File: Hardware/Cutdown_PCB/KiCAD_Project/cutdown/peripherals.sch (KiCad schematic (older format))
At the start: 14 parts, among them Q1 MMBT3904, U2 BMP388, U3 ublox_SAM-M8Q

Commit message: Cutdown PCB Rev 1.0 Complete.
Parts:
- R13: Populated 0 -> 1
- R9: value 10k -> NP
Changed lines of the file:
@@
 AR Path="/5DE92E14/5DE9BB83" Ref="R9"  Part="1"
 F 0 "R9" V 2725 2350 50  0000 L CNN
-F 1 "10k" V 2825 2325 50  0000 L CNN
+F 1 "NP" V 2825 2350 50  0000 L CNN
 F 2 "Resistors_SMD:R_0603_HandSoldering" V 2755 2400 50  0001 C CNN
 F 3 "~" H 2825 2400 50  0001 C CNN
@@
 F 3 "~" H 4725 2250 50  0001 C CNN
 F 4 "1-0000010" H 4725 2250 50  0001 C CNN "Internal Part Number"
-F 5 "0" H 4725 2250 50  0001 C CNN "Populated"
+F 5 "1" H 4725 2250 50  0001 C CNN "Populated"
 	1    4725 2250
 	1    0    0    -1

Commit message: Fix GPS connection to particle.
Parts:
- R10, R11, R12, R13, R9: footprint Resistors_SMD:R_0603_HandSoldering -> Resistor_SMD:R_0603_1608Metric_Pad1.05x0.95mm_HandSolder
- U3: symbol cutdown-rescue:ublox_SAM-M8Q-RF_GPS -> lib_sch:ublox_SAM-M8Q
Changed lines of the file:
@@
 EESchema Schematic File Version 4
-LIBS:cutdown-cache
 EELAYER 30 0
 EELAYER END
@@
 Sheet 2 2
 Title "Cutdown Module - NSSL EFM"
-Date "2019-12-03"
-Rev "1.0"
+Date "2020-03-30"
+Rev "2.0"
 Comp "Leeman Geophysical LLC"
 Comment1 "(479) 373-3736"
@@
 F 0 "R9" V 2725 2350 50  0000 L CNN
 F 1 "NP" V 2825 2350 50  0000 L CNN
-F 2 "Resistors_SMD:R_0603_HandSoldering" V 2755 2400 50  0001 C CNN
+F 2 "Resistor_SMD:R_0603_1608Metric_Pad1.05x0.95mm_HandSolder" V 2755 2400 50  0001 C CNN
 F 3 "~" H 2825 2400 50  0001 C CNN
 F 4 "1-0000010" H 2825 2400 50  0001 C CNN "Internal Part Number"
@@
 F 0 "R10" V 2725 2750 50  0000 L CNN
 F 1 "10k" V 2825 2725 50  0000 L CNN
-F 2 "Resistors_SMD:R_0603_HandSoldering" V 2755 2800 50  0001 C CNN
+F 2 "Resistor_SMD:R_0603_1608Metric_Pad1.05x0.95mm_HandSolder" V 2755 2800 50  0001 C CNN
 F 3 "~" H 2825 2800 50  0001 C CNN
 F 4 "1-0000010" H 2825 2800 50  0001 C CNN "Internal Part Number"
@@
 GPS_TX
 $Comp
-L cutdown-rescue:ublox_SAM-M8Q-RF_GPS U3
+L lib_sch:ublox_SAM-M8Q U3
 U 1 1 5DE9BBA4
 P 7200 2425
@@
 F 0 "R12" V 5700 4550 50  0000 L CNN
 F 1 "1k" V 5775 4550 50  0000 L CNN
-F 2 "Resistors_SMD:R_0603_HandSoldering" V 5705 4600 50  0001 C CNN
+F 2 "Resistor_SMD:R_0603_1608Metric_Pad1.05x0.95mm_HandSolder" V 5705 4600 50  0001 C CNN
 F 3 "~" H 5775 4600 50  0001 C CNN
 F 4 "1-0000013" H 5775 4600 50  0001 C CNN "Internal Part Number"
@@
 F 0 "R11" V 5250 5000 50  0000 L CNN
 F 1 "1k" V 5325 5000 50  0000 L CNN
-F 2 "Resistors_SMD:R_0603_HandSoldering" V 5255 5050 50  0001 C CNN
+F 2 "Resistor_SMD:R_0603_1608Metric_Pad1.05x0.95mm_HandSolder" V 5255 5050 50  0001 C CNN
 F 3 "~" H 5325 5050 50  0001 C CNN
 F 4 "1-0000013" H 5325 5050 50  0001 C CNN "Internal Part Number"
@@
 F 0 "R13" V 4625 2200 50  0000 L CNN
 F 1 "10k" V 4725 2175 50  0000 L CNN
-F 2 "Resistors_SMD:R_0603_HandSoldering" V 4655 2250 50  0001 C CNN
+F 2 "Resistor_SMD:R_0603_1608Metric_Pad1.05x0.95mm_HandSolder" V 4655 2250 50  0001 C CNN
 F 3 "~" H 4725 2250 50  0001 C CNN
 F 4 "1-0000010" H 4725 2250 50  0001 C CNN "Internal Part Number"

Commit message: Rework cutdown schematic for version 2
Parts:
- removed BT1: CR1220, lib_fp:S8411-45R, symbol Device:Battery_Cell
- removed BZ1: Buzzer, lib_fp:PS1240P02BT, symbol Device:Buzzer
- removed C3, C4: 0.1u, Capacitors_SMD:C_0603_HandSoldering, symbol Device:C
- removed Q1: MMBT3904, TO_SOT_Packages_SMD:SOT-23, symbol Transistor_BJT:MMBT3904
- removed R11, R12: 1k, Resistor_SMD:R_0603_1608Metric_Pad1.05x0.95mm_HandSolder, symbol Device:R
- removed U3: ublox_SAM-M8Q, lib_fp:SAM-M8Q, symbol lib_sch:ublox_SAM-M8Q
- added BT? (x2): CR123, symbol Device:Battery_Cell
- added J?: Hot Wire, symbol Connector_Generic:Conn_01x02
- added Q?: FQP30N06L, Package_DirectFET:DirectFET_ST, symbol lib_sch:FQP30N06L
- added R?: 1-0000006, resistors_0603:1-0000006, symbol resistors_0603:1-0000006
- added R?: 1-0000010, resistors_0603:1-0000010, symbol resistors_0603:1-0000010
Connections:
- net labels added: Cutdown_Command
- net labels removed: +BATT, GPS_PPS, GPS_RX, GPS_TX, PIEZO_ELEMENT
- wire segments 30 -> 22
- no-connect marks 5 -> 0
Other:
- note added: "Required mating block\n1-0000784"

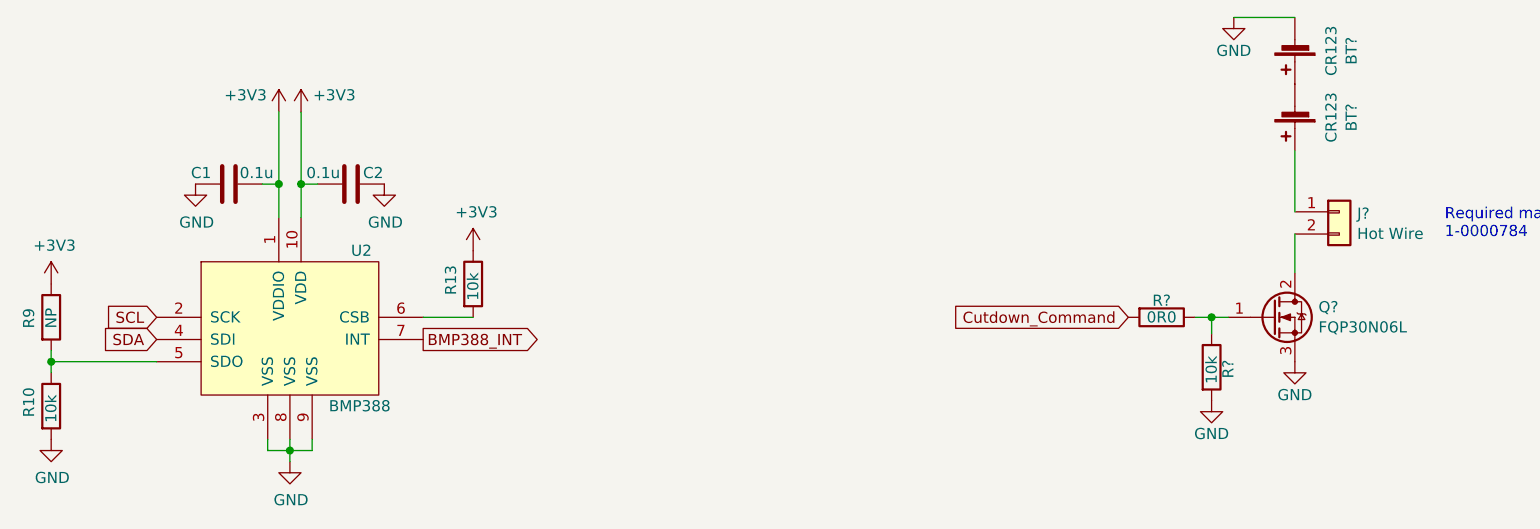
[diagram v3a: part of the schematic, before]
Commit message: Remove cutdown power pcb and update cutdown design
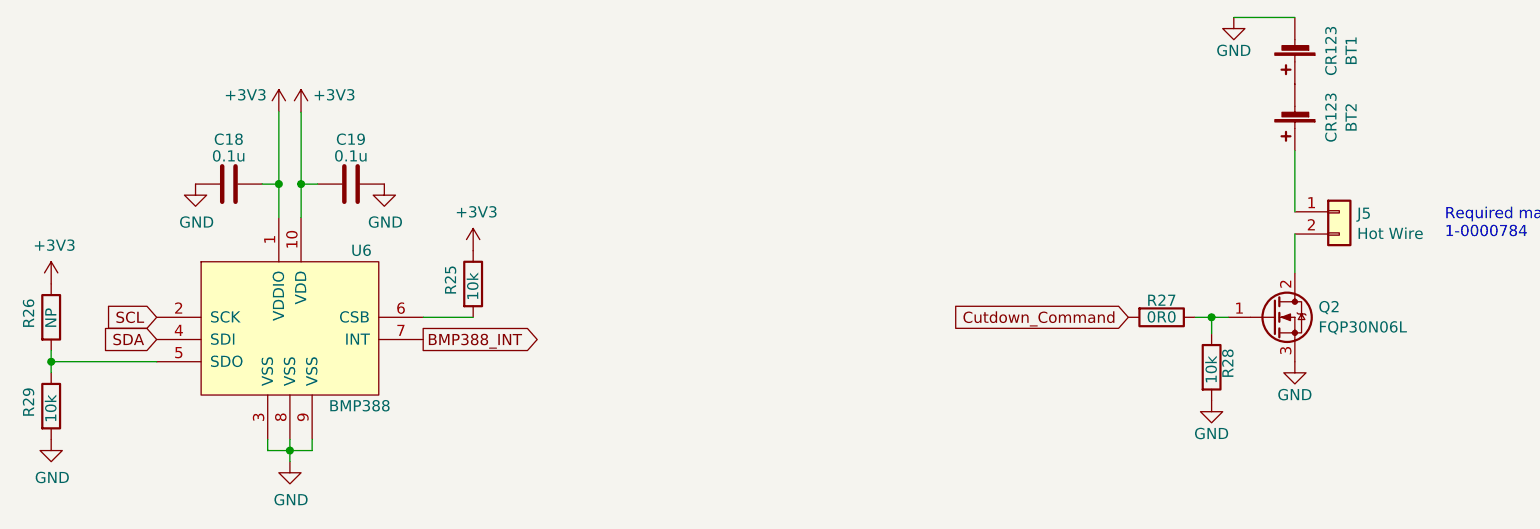
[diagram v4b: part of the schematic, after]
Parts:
- BT1, BT2: renamed from BT?; footprint (none) -> lib_fp:1-0000782
- C18: renamed from C1; footprint Capacitors_SMD:C_0603_HandSoldering -> Capacitor_SMD:C_0603_1608Metric
- C19: renamed from C2; footprint Capacitors_SMD:C_0603_HandSoldering -> Capacitor_SMD:C_0603_1608Metric
- J5: renamed from J?; footprint (none) -> lib_fp:1-0000783
- Q2: renamed from Q?; footprint Package_DirectFET:DirectFET_ST -> Package_TO_SOT_THT:TO-220-3_Horizontal_TabDown; Internal Part Number (none) -> 1-0000449; Populated (none) -> 1
- R25: renamed from R13; footprint Resistor_SMD:R_0603_1608Metric_Pad1.05x0.95mm_HandSolder -> Resistor_SMD:R_0603_1608Metric
- R26: renamed from R9; footprint Resistor_SMD:R_0603_1608Metric_Pad1.05x0.95mm_HandSolder -> Resistor_SMD:R_0603_1608Metric
- R29: renamed from R10; footprint Resistor_SMD:R_0603_1608Metric_Pad1.05x0.95mm_HandSolder -> Resistor_SMD:R_0603_1608Metric
- gave numbers to parts that had none: 2
- renumbered U2 to U6
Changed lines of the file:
@@
 Sheet 2 2
 Title "Cutdown Module - NSSL EFM"
-Date "2020-03-30"
-Rev "2.0"
+Date "2020-12-22"
+Rev "3.0"
 Comp "Leeman Geophysical LLC"
 Comment1 "(479) 373-3736"
@@
 $EndDescr
 $Comp
-L lib_sch:BMP388 U2
+L lib_sch:BMP388 U6
 U 1 1 5DE9BB3A
 P 3900 2450
-F 0 "U2" H 4175 2800 50  0000 L CNN
+F 0 "U6" H 4175 2800 50  0000 L CNN
 F 1 "BMP388" H 4075 2100 50  0000 L CNN
 F 2 "lib_fp:PQFN50P200X200X80-10N" H 3200 2500 50  0001 C CNN
@@
 $EndComp
 $Comp
-L power:+3V3 #PWR0103
+L power:+3V3 #PWR048
 U 1 1 5DE9BB40
 P 3850 1475
-F 0 "#PWR0103" H 3850 1325 50  0001 C CNN
+F 0 "#PWR048" H 3850 1325 50  0001 C CNN
 F 1 "+3V3" H 3700 1550 50  0000 C CNN
 F 2 "" H 3850 1475 50  0001 C CNN
@@
 $EndComp
 $Comp
-L Device:C C2
+L Device:C C19
 U 1 1 5DE9BB48
 P 4175 1800
-F 0 "C2" V 4125 1900 50  0000 C CNN
-F 1 "0.1u" V 4125 1675 50  0000 C CNN
-F 2 "Capacitors_SMD:C_0603_HandSoldering" H 4213 1650 50  0001 C CNN
+F 0 "C19" V 3975 1800 50  0000 C CNN
+F 1 "0.1u" V 4050 1800 50  0000 C CNN
+F 2 "Capacitor_SMD:C_0603_1608Metric" H 4213 1650 50  0001 C CNN
 F 3 "~" H 4175 1800 50  0001 C CNN
 F 4 "1-0000007" H 4175 1800 50  0001 C CNN "Internal Part Number"
@@
 $EndComp
 $Comp
-L Device:C C1
+L Device:C C18
 U 1 1 5DE9BB50
 P 3625 1800
-F 0 "C1" V 3575 1675 50  0000 C CNN
-F 1 "0.1u" V 3575 1925 50  0000 C CNN
-F 2 "Capacitors_SMD:C_0603_HandSoldering" H 3663 1650 50  0001 C CNN
+F 0 "C18" V 3425 1800 50  0000 C CNN
+F 1 "0.1u" V 3500 1800 50  0000 C CNN
+F 2 "Capacitor_SMD:C_0603_1608Metric" H 3663 1650 50  0001 C CNN
 F 3 "~" H 3625 1800 50  0001 C CNN
 F 4 "1-0000007" H 3625 1800 50  0001 C CNN "Internal Part Number"
@@
 Connection ~ 3850 1800
 $Comp
-L power:+3V3 #PWR0104
+L power:+3V3 #PWR049
 U 1 1 5DE9BB5C
 P 3950 1475
-F 0 "#PWR0104" H 3950 1325 50  0001 C CNN
+F 0 "#PWR049" H 3950 1325 50  0001 C CNN
 F 1 "+3V3" H 4100 1550 50  0000 C CNN
 F 2 "" H 3950 1475 50  0001 C CNN
@@
 Connection ~ 3950 1800
 $Comp
-L power:GND #PWR0105
+L power:GND #PWR050
 U 1 1 5DE9BB64
 P 3475 1800
-F 0 "#PWR0105" H 3475 1550 50  0001 C CNN
+F 0 "#PWR050" H 3475 1550 50  0001 C CNN
 F 1 "GND" H 3480 1627 50  0000 C CNN
 F 2 "" H 3475 1800 50  0001 C CNN
@@
 $EndComp
 $Comp
-L power:GND #PWR0106
+L power:GND #PWR051
 U 1 1 5DE9BB6A
 P 4325 1800
-F 0 "#PWR0106" H 4325 1550 50  0001 C CNN
+F 0 "#PWR051" H 4325 1550 50  0001 C CNN
 F 1 "GND" H 4330 1627 50  0000 C CNN
 F 2 "" H 4325 1800 50  0001 C CNN
@@
 SDA
 $Comp
-L power:GND #PWR0107
+L power:GND #PWR057
 U 1 1 5DE9BB73
 P 3900 3050
-F 0 "#PWR0107" H 3900 2800 50  0001 C CNN
+F 0 "#PWR057" H 3900 2800 50  0001 C CNN
 F 1 "GND" H 3905 2877 50  0000 C CNN
 F 2 "" H 3900 3050 50  0001 C CNN
@@
 P 2825 2400
 AR Path="/5DE9BB83" Ref="R?"  Part="1"
-AR Path="/5DE92E14/5DE9BB83" Ref="R9"  Part="1"
-F 0 "R9" V 2725 2350 50  0000 L CNN
+AR Path="/5DE92E14/5DE9BB83" Ref="R26"  Part="1"
+F 0 "R26" V 2725 2350 50  0000 L CNN
 F 1 "NP" V 2825 2350 50  0000 L CNN
-F 2 "Resistor_SMD:R_0603_1608Metric_Pad1.05x0.95mm_HandSolder" V 2755 2400 50  0001 C CNN
+F 2 "Resistor_SMD:R_0603_1608Metric" V 2755 2400 50  0001 C CNN
 F 3 "~" H 2825 2400 50  0001 C CNN
 F 4 "1-0000010" H 2825 2400 50  0001 C CNN "Internal Part Number"
@@
 $EndComp
 $Comp
-L Device:R R10
+L Device:R R29
 U 1 1 5DE9BB8B
 P 2825 2800
-F 0 "R10" V 2725 2750 50  0000 L CNN
+F 0 "R29" V 2725 2750 50  0000 L CNN
 F 1 "10k" V 2825 2725 50  0000 L CNN
-F 2 "Resistor_SMD:R_0603_1608Metric_Pad1.05x0.95mm_HandSolder" V 2755 2800 50  0001 C CNN
+F 2 "Resistor_SMD:R_0603_1608Metric" V 2755 2800 50  0001 C CNN
 F 3 "~" H 2825 2800 50  0001 C CNN
 F 4 "1-0000010" H 2825 2800 50  0001 C CNN "Internal Part Number"
@@
 Connection ~ 2825 2600
 $Comp
-L power:GND #PWR0108
+L power:GND #PWR056
 U 1 1 5DE9BB95
 P 2825 2950
-F 0 "#PWR0108" H 2825 2700 50  0001 C CNN
+F 0 "#PWR056" H 2825 2700 50  0001 C CNN
 F 1 "GND" H 2830 2777 50  0000 C CNN
 F 2 "" H 2825 2950 50  0001 C CNN
@@
 $EndComp
 $Comp
-L power:+3V3 #PWR0109
+L power:+3V3 #PWR053
 U 1 1 5DE9BB9B
 P 2825 2250
-F 0 "#PWR0109" H 2825 2100 50  0001 C CNN
+F 0 "#PWR053" H 2825 2100 50  0001 C CNN
 F 1 "+3V3" H 2840 2423 50  0000 C CNN
 F 2 "" H 2825 2250 50  0001 C CNN
@@
 P 4725 2250
 AR Path="/5DE7F4ED" Ref="R?"  Part="1"
-AR Path="/5DE92E14/5DE7F4ED" Ref="R13"  Part="1"
-F 0 "R13" V 4625 2200 50  0000 L CNN
+AR Path="/5DE92E14/5DE7F4ED" Ref="R25"  Part="1"
+F 0 "R25" V 4625 2200 50  0000 L CNN
 F 1 "10k" V 4725 2175 50  0000 L CNN
-F 2 "Resistor_SMD:R_0603_1608Metric_Pad1.05x0.95mm_HandSolder" V 4655 2250 50  0001 C CNN
+F 2 "Resistor_SMD:R_0603_1608Metric" V 4655 2250 50  0001 C CNN
 F 3 "~" H 4725 2250 50  0001 C CNN
 F 4 "1-0000010" H 4725 2250 50  0001 C CNN "Internal Part Number"
@@
 $EndComp
 $Comp
-L power:+3V3 #PWR0120
+L power:+3V3 #PWR052
 U 1 1 5DE7F4F3
 P 4725 2100
-F 0 "#PWR0120" H 4725 1950 50  0001 C CNN
+F 0 "#PWR052" H 4725 1950 50  0001 C CNN
 F 1 "+3V3" H 4740 2273 50  0000 C CNN
 F 2 "" H 4725 2100 50  0001 C CNN
@@
 	4725 2400 4500 2400
 $Comp
-L Device:Battery_Cell BT?
+L Device:Battery_Cell BT1
 U 1 1 5FDAEB8B
 P 8425 1150
-F 0 "BT?" V 8170 1200 50  0000 C CNN
+F 0 "BT1" V 8170 1200 50  0000 C CNN
 F 1 "CR123" V 8261 1200 50  0000 C CNN
-F 2 "" V 8425 1210 50  0001 C CNN
+F 2 "lib_fp:1-0000782" V 8425 1210 50  0001 C CNN
 F 3 "~" V 8425 1210 50  0001 C CNN
 F 4 "1-0000782" H 8425 1150 50  0001 C CNN "Internal Part Number"
@@
 $EndComp
 $Comp
-L resistors_0603:1-0000006 R?
+L resistors_0603:1-0000006 R27
 U 1 1 5FDB2113
 P 7825 2400
-F 0 "R?" V 7750 2400 50  0000 C CNN
+F 0 "R27" V 7750 2400 50  0000 C CNN
 F 1 "1-0000006" V 7825 2400 50  0001 C CNN
 F 2 "resistors_0603:1-0000006" V 7755 2400 50  0001 C CNN
@@
 $EndComp
 $Comp
-L resistors_0603:1-0000010 R?
+L resistors_0603:1-0000010 R28
 U 1 1 5FDB2B0F
 P 8050 2625
-F 0 "R?" V 8125 2575 50  0000 L CNN
+F 0 "R28" V 8125 2575 50  0000 L CNN
 F 1 "1-0000010" V 8050 2625 50  0001 C CNN
 F 2 "resistors_0603:1-0000010" V 7980 2625 50  0001 C CNN
@@
 $EndComp
 $Comp
-L lib_sch:FQP30N06L Q?
+L lib_sch:FQP30N06L Q2
 U 1 1 5FDB4039
 P 8325 2400
-F 0 "Q?" H 8531 2446 50  0000 L CNN
+F 0 "Q2" H 8531 2446 50  0000 L CNN
 F 1 "FQP30N06L" H 8531 2355 50  0000 L CNN
-F 2 "Package_DirectFET:DirectFET_ST" H 8325 2400 50  0001 C CIN
+F 2 "Package_TO_SOT_THT:TO-220-3_Horizontal_TabDown" H 8325 2400 50  0001 C CIN
 F 3 "https://www.infineon.com/dgdl/Infineon-BSF450NE7NH3-DS-v02_02-EN.pdf?fileId=db3a30433a047ba0013a687e2ae403da" H 8325 2400 50  0001 L CNN
+F 4 "1-0000449" H 8325 2400 50  0001 C CNN "Internal Part Number"
+F 5 "1" H 8325 2400 50  0001 C CNN "Populated"
 	1    8325 2400
 	1    0    0    -1
 $EndComp
 $Comp
-L power:GND #PWR?
+L power:GND #PWR054
 U 1 1 5FDB4AF1
 P 8425 2600
-F 0 "#PWR?" H 8425 2350 50  0001 C CNN
+F 0 "#PWR054" H 8425 2350 50  0001 C CNN
 F 1 "GND" H 8425 2450 50  0000 C CNN
 F 2 "" H 8425 2600 50  0001 C CNN
@@
 	8050 2400 8125 2400
 $Comp
-L power:GND #PWR?
+L power:GND #PWR055
 U 1 1 5FDB62BA
 P 8050 2775
-F 0 "#PWR?" H 8050 2525 50  0001 C CNN
+F 0 "#PWR055" H 8050 2525 50  0001 C CNN
 F 1 "GND" H 8050 2625 50  0000 C CNN
 F 2 "" H 8050 2775 50  0001 C CNN
@@
 $EndComp
 $Comp
-L Connector_Generic:Conn_01x02 J?
+L Connector_Generic:Conn_01x02 J5
 U 1 1 5FDB68FF
 P 8625 1925
-F 0 "J?" H 8705 1917 50  0000 L CNN
+F 0 "J5" H 8705 1917 50  0000 L CNN
 F 1 "Hot Wire" H 8705 1826 50  0000 L CNN
-F 2 "" H 8625 1925 50  0001 C CNN
+F 2 "lib_fp:1-0000783" H 8625 1925 50  0001 C CNN
 F 3 "~" H 8625 1925 50  0001 C CNN
 F 4 "1-0000783" H 8625 1925 50  0001 C CNN "Internal Part Number"
@@
 Cutdown_Command
 $Comp
-L Device:Battery_Cell BT?
+L Device:Battery_Cell BT2
 U 1 1 5FE233BE
 P 8425 1450
-F 0 "BT?" V 8170 1500 50  0000 C CNN
+F 0 "BT2" V 8170 1500 50  0000 C CNN
 F 1 "CR123" V 8261 1500 50  0000 C CNN
-F 2 "" V 8425 1510 50  0001 C CNN
+F 2 "lib_fp:1-0000782" V 8425 1510 50  0001 C CNN
 F 3 "~" V 8425 1510 50  0001 C CNN
 F 4 "1-0000782" H 8425 1450 50  0001 C CNN "Internal Part Number"
@@
 $EndComp
 $Comp
-L power:GND #PWR?
+L power:GND #PWR047
 U 1 1 5FE23F21
 P 8150 1050
-F 0 "#PWR?" H 8150 800 50  0001 C CNN
+F 0 "#PWR047" H 8150 800 50  0001 C CNN
 F 1 "GND" H 8150 900 50  0000 C CNN
 F 2 "" H 8150 1050 50  0001 C CNN

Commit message: Tweaks
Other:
- note added: "Required mating block\n1-0000797"
- note removed: "Required mating block\n1-0000784"
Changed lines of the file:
@@
 	8150 1050 8425 1050
 Text Notes 9100 2050 0    50   ~ 0
-Required mating block\n1-0000784
+Required mating block\n1-0000797
 $EndSCHEMATC

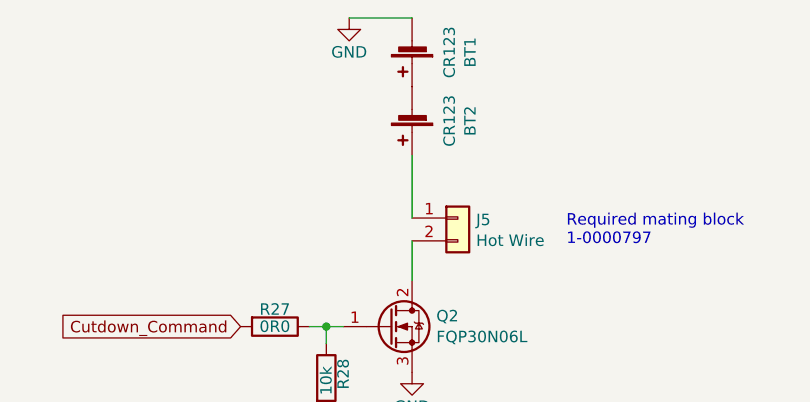
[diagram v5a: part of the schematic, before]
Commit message: Move batteries, remove charging circuit, add mounting holes.
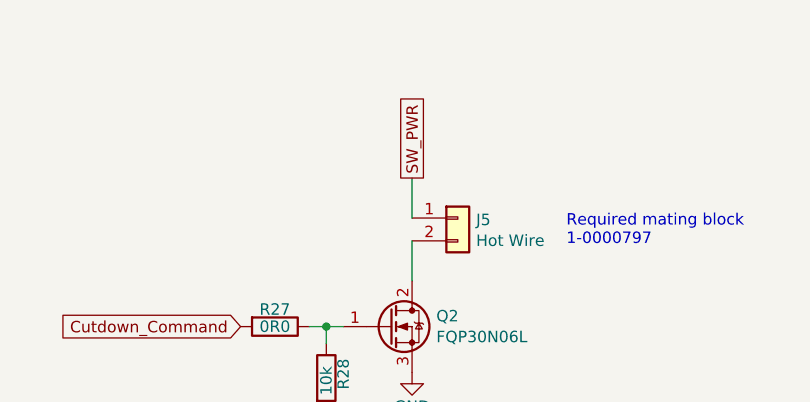
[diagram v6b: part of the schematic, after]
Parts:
- removed BT1, BT2: CR123, lib_fp:1-0000782, symbol Device:Battery_Cell
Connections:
- net SW_PWR: now reaches J5.1 (Pin_1)
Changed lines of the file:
@@
 	4725 2400 4500 2400
-$Comp
-L Device:Battery_Cell BT1
-U 1 1 5FDAEB8B
-P 8425 1150
-F 0 "BT1" V 8170 1200 50  0000 C CNN
-F 1 "CR123" V 8261 1200 50  0000 C CNN
-F 2 "lib_fp:1-0000782" V 8425 1210 50  0001 C CNN
-F 3 "~" V 8425 1210 50  0001 C CNN
-F 4 "1-0000782" H 8425 1150 50  0001 C CNN "Internal Part Number"
-F 5 "1" H 8425 1150 50  0001 C CNN "Populated"
-	1    8425 1150
-	-1   0    0    1
-$EndComp
 $Comp
 L resistors_0603:1-0000006 R27
@@
 	1    0    0    -1
 $EndComp
+Wire Wire Line
+	8425 2200 8425 2025
+Text GLabel 7675 2400 0    50   Input ~ 0
+Cutdown_Command
+Text Notes 9100 2050 0    50   ~ 0
+Required mating block\n1-0000797
 $Comp
 L Connector_Generic:Conn_01x02 J5
@@
 $EndComp
 Wire Wire Line
-	8425 2200 8425 2025
-Wire Wire Line
-	8425 1650 8425 1925
-Text GLabel 7675 2400 0    50   Input ~ 0
-Cutdown_Command
-$Comp
-L Device:Battery_Cell BT2
-U 1 1 5FE233BE
-P 8425 1450
-F 0 "BT2" V 8170 1500 50  0000 C CNN
-F 1 "CR123" V 8261 1500 50  0000 C CNN
-F 2 "lib_fp:1-0000782" V 8425 1510 50  0001 C CNN
-F 3 "~" V 8425 1510 50  0001 C CNN
-F 4 "1-0000782" H 8425 1450 50  0001 C CNN "Internal Part Number"
-F 5 "1" H 8425 1450 50  0001 C CNN "Populated"
-	1    8425 1450
-	-1   0    0    1
-$EndComp
-$Comp
-L power:GND #PWR047
-U 1 1 5FE23F21
-P 8150 1050
-F 0 "#PWR047" H 8150 800 50  0001 C CNN
-F 1 "GND" H 8150 900 50  0000 C CNN
-F 2 "" H 8150 1050 50  0001 C CNN
-F 3 "" H 8150 1050 50  0001 C CNN
-	1    8150 1050
-	1    0    0    -1
-$EndComp
-Wire Wire Line
-	8150 1050 8425 1050
-Text Notes 9100 2050 0    50   ~ 0
-Required mating block\n1-0000797
+	8425 1750 8425 1925
+Text GLabel 8425 1750 1    50   UnSpc ~ 0
+SW_PWR
 $EndSCHEMATC
